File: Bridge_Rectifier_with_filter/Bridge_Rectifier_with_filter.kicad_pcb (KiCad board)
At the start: 4 copper layers, 28 x 22.5 mm, 13 parts, among them J1 Screw_Terminal_01x02, J2 Conn_01x02_Pin, T1 Transformer_1P_1S

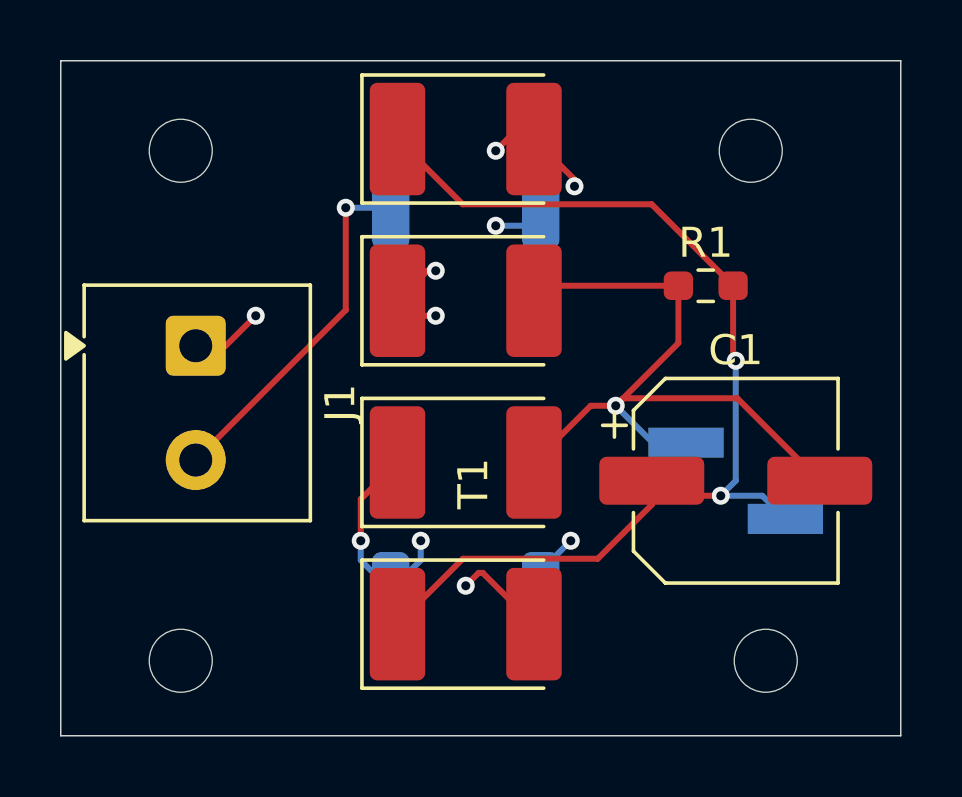
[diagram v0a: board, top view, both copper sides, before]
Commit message: Through holes changes to buried
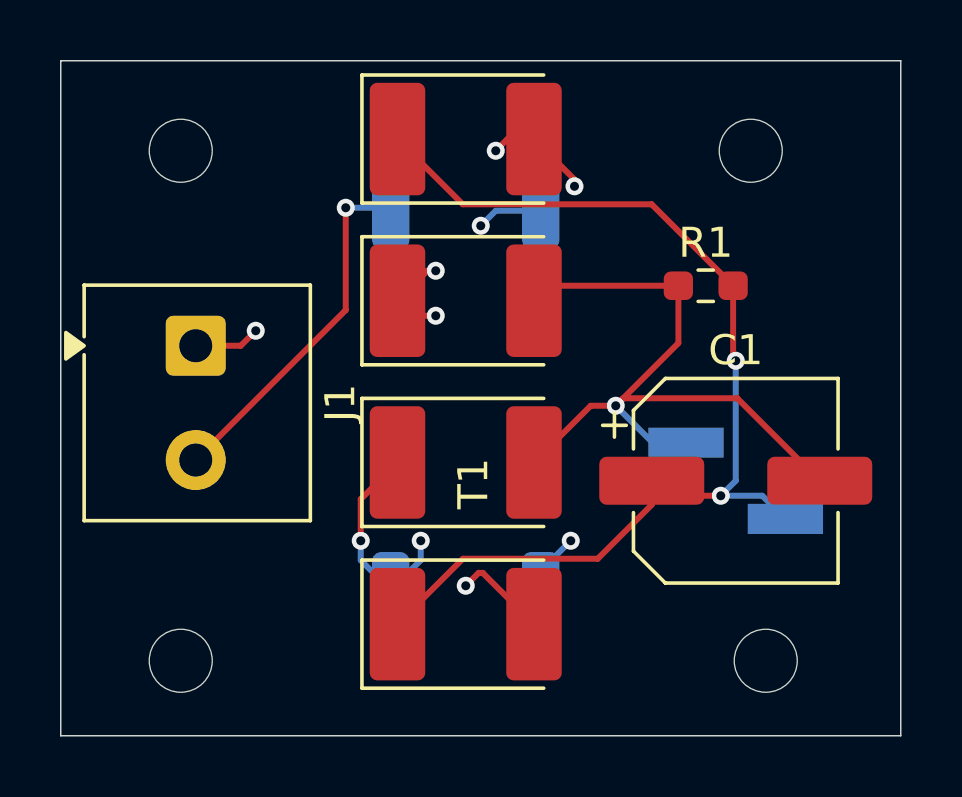
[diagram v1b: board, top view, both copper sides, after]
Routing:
- net Net-(J1-Pin_1): track 13.4 -> 14.1 mm
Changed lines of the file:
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@@
 		(net "Net-(D1-A)")
 	)
-	(via
+	(via buried
 		(at 112.625 58.685)
 		(size 0.6)
 		(drill 0.3)
-		(layers "F.Cu" "B.Cu")
-		(net "Net-(D1-A)")
-	)
-	(via
-		(at 112.5 70.5)
-		(size 0.6)
-		(drill 0.3)
-		(layers "F.Cu" "B.Cu")
-		(net "Net-(D1-A)")
-	)
-	(via
+		(layers "F.Cu" "In1.Cu")
+		(net "Net-(D1-A)")
+	)
+	(via buried
 		(at 110 57.5)
 		(size 0.6)
 		(drill 0.3)
-		(layers "F.Cu" "B.Cu")
-		(net "Net-(D1-A)")
-	)
-	(via
+		(layers "F.Cu" "In2.Cu")
+		(net "Net-(D1-A)")
+	)
+	(via buried
 		(at 108 63)
 		(size 0.6)
 		(drill 0.3)
-		(layers "F.Cu" "B.Cu")
-		(net "Net-(D1-A)")
-	)
-	(via
+		(layers "F.Cu" "In1.Cu")
+		(net "Net-(D1-A)")
+	)
+	(via buried
 		(at 108 61.5)
 		(size 0.6)
 		(drill 0.3)
-		(layers "F.Cu" "B.Cu")
+		(layers "F.Cu" "In2.Cu")
 		(net "Net-(D1-A)")
 	)
@@
 		(net "Net-(D1-A)")
 	)
+	(via buried
+		(at 112.5 70.5)
+		(size 0.6)
+		(drill 0.3)
+		(layers "In1.Cu" "B.Cu")
+		(net "Net-(D1-A)")
+	)
 	(segment
 		(start 108 59.5)
@@
 		(net "Net-(D3-K)")
 	)
-	(via
+	(via buried
 		(at 109 72)
 		(size 0.6)
 		(drill 0.3)
-		(layers "F.Cu" "B.Cu")
-		(net "Net-(D3-K)")
-	)
-	(via
-		(at 107.5 70.5)
-		(size 0.6)
-		(drill 0.3)
-		(layers "F.Cu" "B.Cu")
+		(layers "F.Cu" "In2.Cu")
 		(net "Net-(D3-K)")
 	)
@@
 		(net "Net-(D3-K)")
 	)
+	(via buried
+		(at 107.5 70.5)
+		(size 0.6)
+		(drill 0.3)
+		(layers "In2.Cu" "B.Cu")
+		(net "Net-(D3-K)")
+	)
 	(segment
 		(start 114.25 65.75)
@@
 	)
 	(segment
-		(start 101 64)
-		(end 102 63)
-		(width 0.2)
-		(layer "F.Cu")
-		(net "Net-(J1-Pin_1)")
-	)
-	(segment
 		(start 100 64)
-		(end 101 64)
-		(width 0.2)
-		(layer "F.Cu")
-		(net "Net-(J1-Pin_1)")
-	)
-	(via
-		(at 102 63)
-		(size 0.6)
-		(drill 0.3)
-		(layers "F.Cu" "B.Cu")
-		(net "Net-(J1-Pin_1)")
-	)
-	(via
-		(at 110 60)
-		(size 0.6)
-		(drill 0.3)
-		(layers "F.Cu" "B.Cu")
-		(net "Net-(J1-Pin_1)")
-	)
-	(segment
-		(start 110 60)
-		(end 111 60)
+		(end 101.5 64)
+		(width 0.2)
+		(layer "F.Cu")
+		(net "Net-(J1-Pin_1)")
+	)
+	(segment
+		(start 101.5 64)
+		(end 102 63.5)
+		(width 0.2)
+		(layer "F.Cu")
+		(net "Net-(J1-Pin_1)")
+	)
+	(via buried
+		(at 102 63.5)
+		(size 0.6)
+		(drill 0.3)
+		(layers "F.Cu" "In1.Cu")
+		(net "Net-(J1-Pin_1)")
+	)
+	(segment
+		(start 111.5 59.5)
+		(end 110 59.5)
+		(width 0.2)
+		(layer "B.Cu")
+		(net "Net-(J1-Pin_1)")
+	)
+	(segment
+		(start 110 59.5)
+		(end 109.5 60)
 		(width 0.2)
 		(layer "B.Cu")
@@
 	)
 	(segment
-		(start 105 60)
-		(end 110 60)
-		(width 0.2)
-		(layer "In1.Cu")
-		(net "Net-(J1-Pin_1)")
-	)
-	(segment
-		(start 102 63)
-		(end 105 60)
-		(width 0.2)
-		(layer "In1.Cu")
-		(net "Net-(J1-Pin_1)")
-	)
+		(start 102 63.5)
+		(end 105.5 60)
+		(width 0.2)
+		(layer "In1.Cu")
+		(net "Net-(J1-Pin_1)")
+	)
+	(segment
+		(start 105.5 60)
+		(end 109.5 60)
+		(width 0.2)
+		(layer "In1.Cu")
+		(net "Net-(J1-Pin_1)")
+	)
+	(via blind
+		(at 109.5 60)
+		(size 0.6)
+		(drill 0.3)
+		(layers "In1.Cu" "B.Cu")
+		(net "Net-(J1-Pin_1)")
+	)

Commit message: xenor regulator added in the bridge rectifier
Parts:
- added D5: D_Zener, Diode_SMD:D_SOD-323, F.Cu at (120.7, 62.0)
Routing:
- net Net-(D2-A): track 24.3 -> 29.6 mm
- net Net-(D1-K): track 36.4 -> 38.1 mm

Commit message: new clipper and clamper circuits are added
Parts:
- removed H1, H2, H3, H4: MountingHole, MountingHole:MountingHole_2.1mm
- added R2: R, Resistor_SMD:R_0603_1608Metric_Pad0.98x0.95mm_HandSolder, B.Cu at (115.3, 63.8)
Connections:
- D5 pad 1: Net-(D1-K) -> Net-(D5-K)
- J2 pad 2: Net-(D1-K) -> Net-(D5-K)
- R1 pad 2: Net-(D1-K) -> Net-(D5-K)
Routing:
- net Net-(D5-K): track 0.00 -> 22.5 mm, vias 0 -> 1
- net Net-(D1-K): track 38.1 -> 35.6 mm, vias 2 -> 3
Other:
- outline, holes or cut-outs redrawn
